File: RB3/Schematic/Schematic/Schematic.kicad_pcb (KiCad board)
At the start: 2 copper layers, 6 parts, among them J4 ESC, J5 ESC_PWR, SW1 MAIN_CUTOFF, U3 Mini360

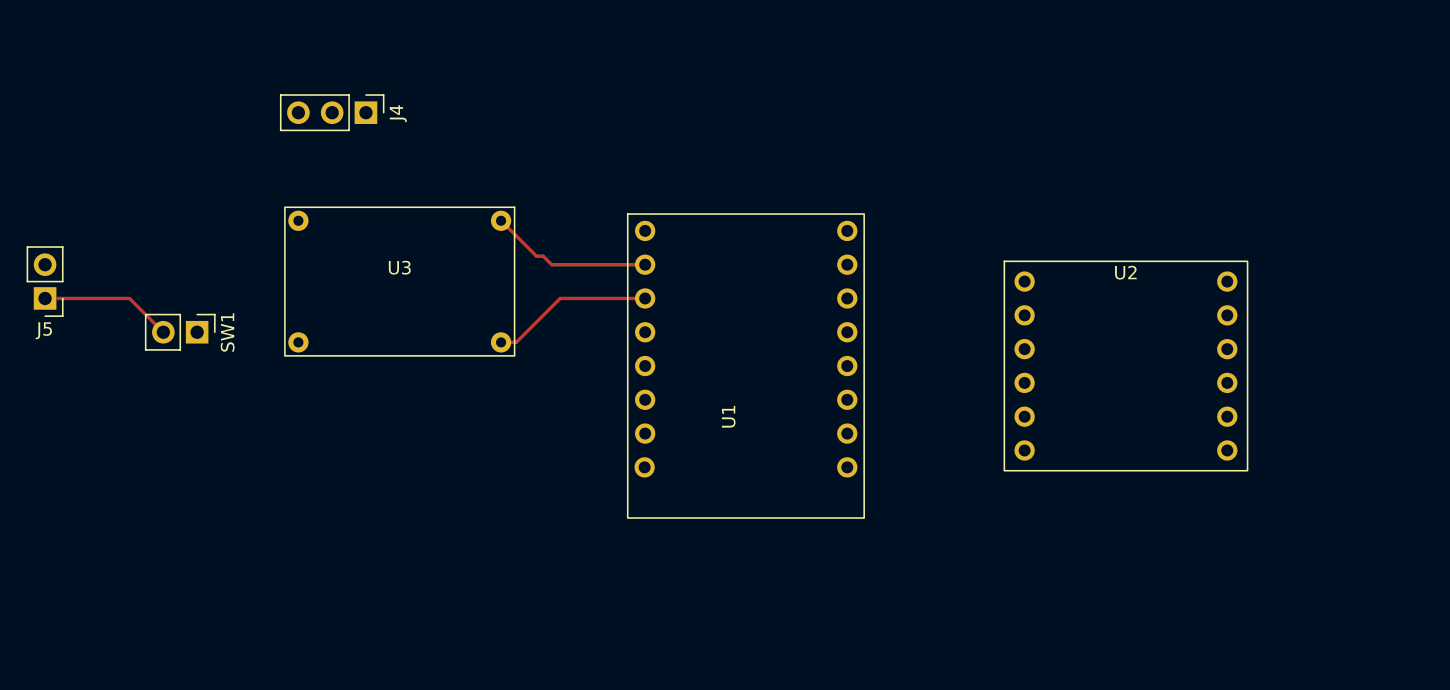
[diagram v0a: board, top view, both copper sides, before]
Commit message: lots of CAD and firmware work
back to basics: re-establish communication between two ESP32s because that was broken in the higher-level code.
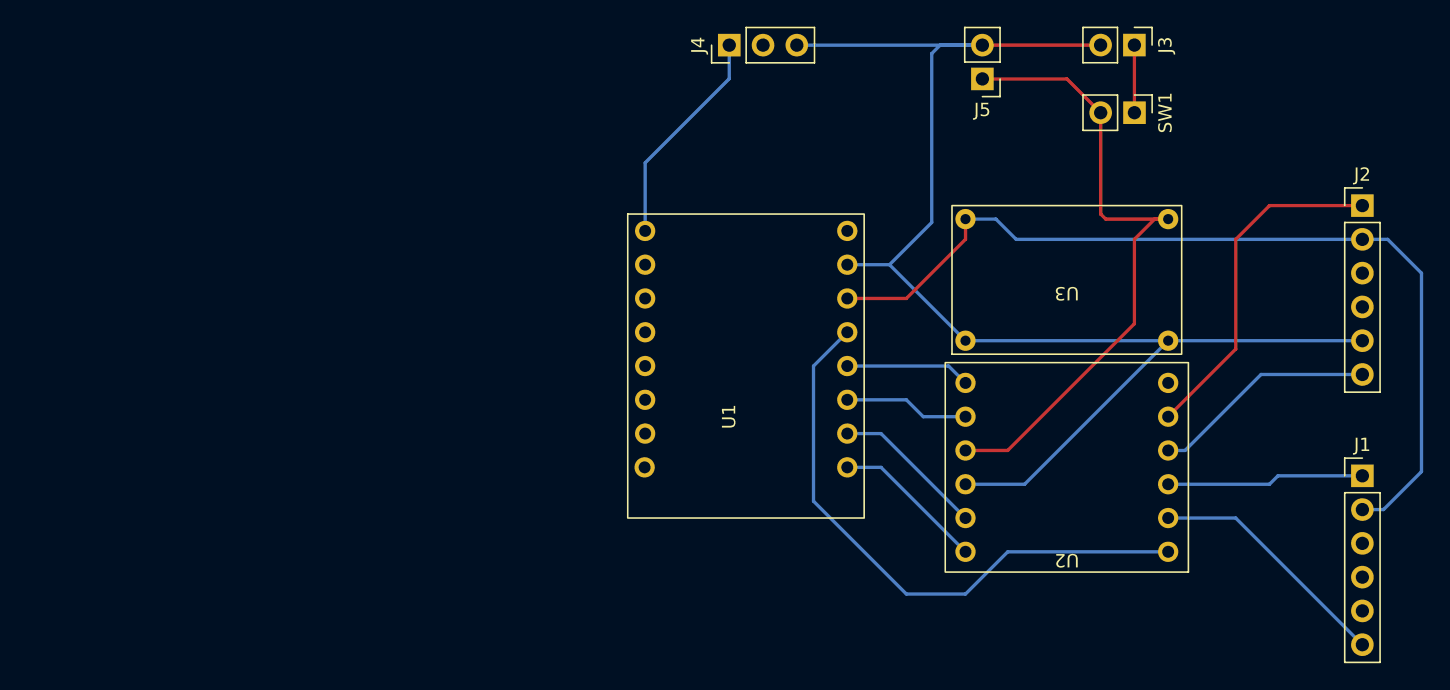
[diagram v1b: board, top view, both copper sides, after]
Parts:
- added J1: Motor 1, Connector_PinHeader_2.54mm:PinHeader_1x06_P2.54mm_Vertical, F.Cu at (153.0, 76.2)
- added J2: Motor 1, Connector_PinHeader_2.54mm:PinHeader_1x06_P2.54mm_Vertical, F.Cu at (153.0, 55.9)
- added J3: Battery, Connector_PinHeader_2.54mm:PinHeader_1x02_P2.54mm_Vertical, F.Cu at (135.9, 43.8)
- moved SW1 72.4 mm to (135.9, 48.9)
- moved J5 72.4 mm to (124.5, 46.4)
- moved U3 50.2 mm to (130.8, 61.5), turned to 180 degrees
- moved J4 27.8 mm to (105.4, 43.8), turned to 90 degrees
- moved U2 11.1 mm to (130.8, 76.8), turned to 180 degrees
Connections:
- U1 pad 1: unconnected-(U1-5v5-Pad1) -> /ESC
- U1 pad 10: unconnected-(U1-D20/RX-Pad10) -> /M1 Control B
- U1 pad 11: unconnected-(U1-D10-Pad11) -> /M2 Control A
- U1 pad 12: /M2 EB -> /M2 Control B
- U1 pad 13: /M2 EA -> /SLEEP
- U1 pad 14: /M1 EB -> +3.3V
- U1 pad 15: /M1 EA -> GND
- U1 pad 16: /ESC -> unconnected-(U1-5v5-Pad16)
- U1 pad 2: GND -> /M2 EB
- U1 pad 3: +3.3V -> /M2 EA
- U1 pad 4: /SLEEP -> /M1 EB
- U1 pad 5: /M1 Control A -> /M1 EA
- U1 pad 6: /M1 Control B -> unconnected-(U1-D10-Pad6)
- U1 pad 7: /M2 Control A -> unconnected-(U1-D20/RX-Pad7)
- U1 pad 8: /M2 Control B -> unconnected-(U1-D21/TX-Pad8)
- U1 pad 9: unconnected-(U1-D21/TX-Pad9) -> /M1 Control A
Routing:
- net GND: track 12.2 -> 104.9 mm
- net +3.3V: track 12.2 -> 68.8 mm
- net /SLEEP: track 0.00 -> 44.6 mm
- net /+BATT SW: track 9.95 -> 49.0 mm
- net /M2 A: track 0.00 -> 26.0 mm
- net /M1 B: track 0.00 -> 18.6 mm
- net /M2 B: track 0.00 -> 17.0 mm
- net /ESC: track 0.00 -> 16.6 mm
- net /M1 A: track 0.00 -> 14.9 mm
- net /M1 Control A: track 0.00 -> 11.5 mm
- net /M1 Control B: track 0.00 -> 11.5 mm
- net /M2 Control B: track 0.00 -> 9.42 mm
- net /M2 Control A: track 0.00 -> 9.42 mm
- net +BATT: track 0.00 -> 5.09 mm
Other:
- board text added: "M1 - WHITE GND - BLUE C1 - GREEN C2 - YELLOW VCC - BLACK M2 - RED"
